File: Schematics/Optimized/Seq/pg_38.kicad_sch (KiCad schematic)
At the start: 67 parts, among them U3901 XBUF64, U3902 XBUF64, U7803 F86

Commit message: Integrate SEQ condensations
Tested: passed expmon_test_seq
Tested: passed run_udiag
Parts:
- renumbered U7803 to U2401
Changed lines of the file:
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@@
   (symbol (lib_id "r1000:F86") (at 482.6 48.26 0) (unit 1)
     (in_bom yes) (on_board yes) (dnp no)
-    (property "Reference" "U7803" (at 495.3 45.72 0)
+    (property "Reference" "U2401" (at 495.3 45.72 0)
       (effects (font (size 1.27 1.27)))
     )
@@
     (instances
       (project "SEQ"
-        (path "/20011966-1ffc-24d7-1b4b-436a182362c4/20011966-47af-2163-0df3-3d84c5f3c1ad"
-          (reference "U7803") (unit 1)
-        )
         (path "/20011966-1ffc-24d7-1b4b-436a182362c4/20011966-7b9d-2905-5287-11179446946c"
           (reference "U2401") (unit 1)

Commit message: Merge SEQ changes
Tested: passed run_udiag
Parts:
- added GF140, GF142, GF144, GF146, GF160, GF162, GF164, GF166, GF296: GF, symbol r1000:GF
- added U4010: F521, symbol r1000:F521
- added U4011: F51, symbol r1000:F51
- added U4012: F37, symbol r1000:F37
- added U5: F244, symbol r1000:F244
- added U6: XPAR64, symbol r1000:XPAR64
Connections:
- net PD: now also U4010.1 (E), U6.1 (ODD)
- net TYPE_DRV~: now also U4012.3 (Q), U5.1 (OE0), U5.19 (OE1)
- net TYPE~0: now also U6.2 (I0)
- net TYPE~1: now also U6.3 (I1)
- net TYPE~10: now also U6.12 (I10)
- net TYPE~11: now also U6.13 (I11)
- net TYPE~12: now also U6.14 (I12)
- net TYPE~13: now also U6.15 (I13)
- net TYPE~14: now also U6.16 (I14)
- net TYPE~15: now also U6.17 (I15)
- net TYPE~16: now also U6.18 (I16)
- net TYPE~17: now also U6.19 (I17)
- net TYPE~18: now also U6.20 (I18)
- net TYPE~19: now also U6.21 (I19)
- net TYPE~2: now also U6.4 (I2)
- net TYPE~20: now also U6.22 (I20)
- net TYPE~21: now also U6.23 (I21)
- net TYPE~22: now also U6.24 (I22)
- net TYPE~23: now also U6.25 (I23)
- net TYPE~24: now also U6.26 (I24)
- net TYPE~25: now also U6.27 (I25)
- net TYPE~26: now also U6.28 (I26)
- net TYPE~27: now also U6.29 (I27)
- net TYPE~28: now also U6.30 (I28)
- net TYPE~29: now also U6.31 (I29)
- net TYPE~3: now also U6.5 (I3)
- net TYPE~30: now also U6.32 (I30)
- net TYPE~31: now also U6.33 (I31)
- net TYPE~32: now also U6.34 (I32)
- net TYPE~33: now also U6.35 (I33)
- net TYPE~34: now also U6.36 (I34)
- net TYPE~35: now also U6.37 (I35)
- net TYPE~36: now also U6.38 (I36)
- net TYPE~37: now also U6.39 (I37)
- net TYPE~38: now also U6.40 (I38)
- net TYPE~39: now also U6.41 (I39)
- net TYPE~4: now also U6.6 (I4)
- net TYPE~40: now also U6.42 (I40)
- net TYPE~41: now also U6.43 (I41)
- net TYPE~42: now also U6.44 (I42)
- net TYPE~43: now also U6.45 (I43)
- net TYPE~44: now also U6.46 (I44)
- net TYPE~45: now also U6.47 (I45)
- net TYPE~46: now also U6.48 (I46)
- net TYPE~47: now also U6.49 (I47)
- net TYPE~48: now also U6.50 (I48)
- net TYPE~49: now also U6.51 (I49)
- net TYPE~5: now also U6.7 (I5)
- net TYPE~50: now also U6.52 (I50)
- net TYPE~51: now also U6.53 (I51)
- net TYPE~52: now also U6.54 (I52)
- net TYPE~53: now also U6.55 (I53)
- net TYPE~54: now also U6.56 (I54)
- net TYPE~55: now also U6.57 (I55)
- net TYPE~56: now also U6.58 (I56)
- net TYPE~57: now also U6.59 (I57)
- net TYPE~58: now also U6.60 (I58)
- net TYPE~59: now also U6.61 (I59)
- net TYPE~6: now also U6.8 (I6)
- net TYPE~60: now also U6.62 (I60)
- net TYPE~61: now also U6.63 (I61)
- net TYPE~62: now also U6.64 (I62)
- net TYPE~63: now also U6.65 (I63)
- net TYPE~7: now also U6.9 (I7)
- net TYPE~8: now also U6.10 (I8)
- net TYPE~9: now also U6.11 (I9)
- new net: U4011.7 (Q), U4012.1 (D0)
- new net BUS_OFF.DIAG: U4011.6 (B3)
- new net Q.SEQ_TV.EN~: GF296.1, U4011.1 (A1)
- new net Q.TYPE.P0: GF166.1, U4010.2 (A0), U5.18 (Y0)
- new net Q.TYPE.P1: GF164.1, U4010.4 (A1), U5.16 (Y1)
- new net Q.TYPE.P2: GF162.1, U4010.6 (A2), U5.14 (Y2)
- new net Q.TYPE.P3: GF160.1, U4010.8 (A3), U5.12 (Y3)
- new net Q.TYPE.P4: GF146.1, U4010.11 (A4), U5.9 (Y4)
- new net Q.TYPE.P5: GF144.1, U4010.13 (A5), U5.7 (Y5)
- new net Q.TYPE.P6: GF142.1, U4010.15 (A6), U5.5 (Y6)
- new net Q.TYPE.P7: GF140.1, U4010.17 (A7), U5.3 (Y7)
- new net Q1~: U4012.2 (D1)
- new net TYPE_POD0: U4010.3 (B0), U5.2 (I0), U6.66 (P0)
- new net TYPE_POD1: U4010.5 (B1), U5.4 (I1), U6.67 (P1)
- new net TYPE_POD2: U4010.7 (B2), U5.6 (I2), U6.68 (P2)
- new net TYPE_POD3: U4010.9 (B3), U5.8 (I3), U6.69 (P3)
- new net TYPE_POD4: U4010.12 (B4), U5.11 (I4), U6.70 (P4)
- new net TYPE_POD5: U4010.14 (B5), U5.13 (I5), U6.71 (P5)
- new net TYPE_POD6: U4010.16 (B6), U5.15 (I6), U6.72 (P6)
- new net TYPE_POD7: U4010.18 (B7), U5.17 (I7), U6.73 (P7)
- new net TYP_ON.DIAG~: U4011.3 (A3), U4011.4 (B1)
- new net TYP_PERR.MCHK: U4010.19 (A=B)
- no-connect marks 0 -> 3
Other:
- moved on the sheet: GF108, GF110, GF112, GF114, GF12, GF124, GF126, GF128, GF130, GF14, GF16, GF176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

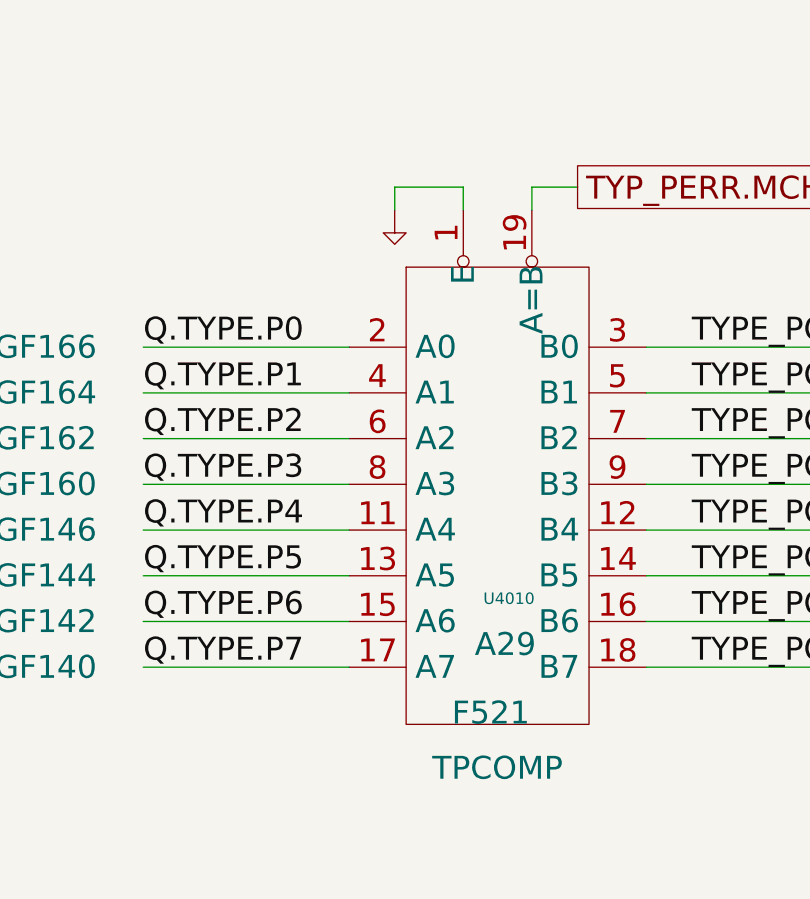
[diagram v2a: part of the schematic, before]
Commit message: Condensation of SEQ, TYP & VAL conditions
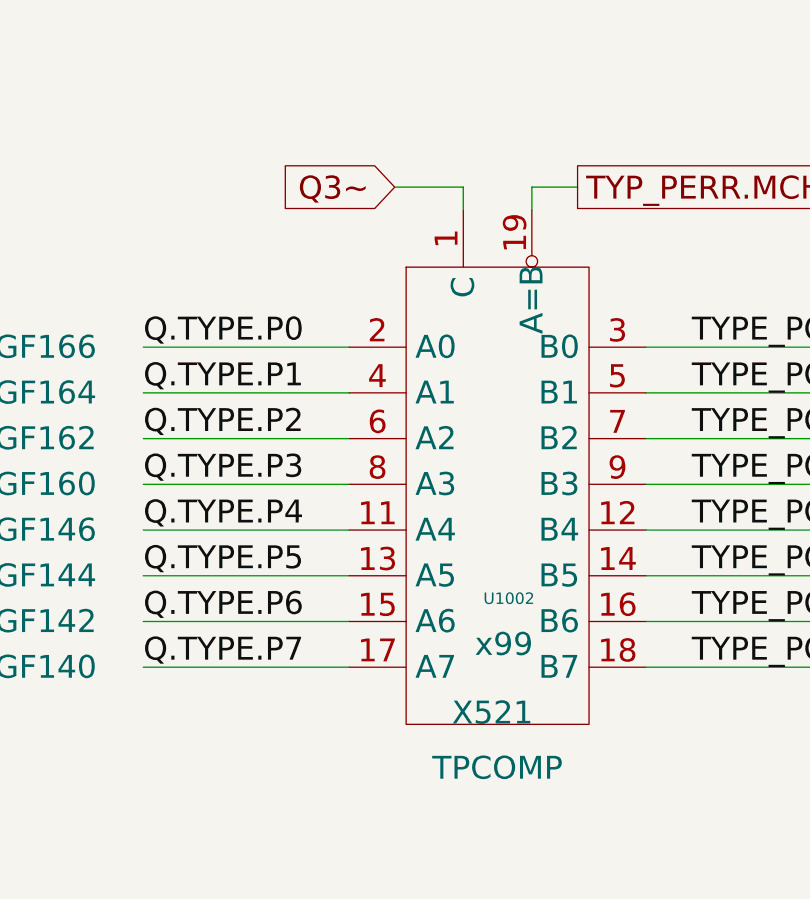
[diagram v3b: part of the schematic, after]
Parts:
- removed U4010: F521, symbol r1000:F521
- added U1002: X521, symbol r1000:X521
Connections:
- net Q.TYPE.P0: now also U1002.2 (A0)
- net Q.TYPE.P1: now also U1002.4 (A1)
- net Q.TYPE.P2: now also U1002.6 (A2)
- net Q.TYPE.P3: now also U1002.8 (A3)
- net Q.TYPE.P4: now also U1002.11 (A4)
- net Q.TYPE.P5: now also U1002.13 (A5)
- net Q.TYPE.P6: now also U1002.15 (A6)
- net Q.TYPE.P7: now also U1002.17 (A7)
- net TYPE_POD0: now also U1002.3 (B0)
- net TYPE_POD1: now also U1002.5 (B1)
- net TYPE_POD2: now also U1002.7 (B2)
- net TYPE_POD3: now also U1002.9 (B3)
- net TYPE_POD4: now also U1002.12 (B4)
- net TYPE_POD5: now also U1002.14 (B5)
- net TYPE_POD6: now also U1002.16 (B6)
- net TYPE_POD7: now also U1002.18 (B7)
- net TYP_PERR.MCHK: now also U1002.19 (A=B)
- new net Q3~: U1002.1 (C)
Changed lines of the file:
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@@
     (stroke (width 0) (type default))
   )
-  (wire (pts (xy 492.76 109.22) (xy 492.76 106.68))
-    (stroke (width 0) (type default))
-  )
   (wire (pts (xy 139.7 109.22) (xy 109.22 109.22))
     (stroke (width 0) (type default))
@@
     )
   )
+  (global_label "Q3~" (shape input) (at 492.76 106.68 180) (fields_autoplaced)
+    (effects (font (size 2.54 2.54)) (justify right))
+    (property "Intersheetrefs" "${INTERSHEET_REFS}" (at 479.8647 106.68 0)
+      (effects (font (size 1.27 1.27)) (justify right))
+    )
+  )
   (global_label "TYP_PERR.MCHK" (shape output) (at 513.08 106.68 0) (fields_autoplaced)
     (effects (font (size 2.54 2.54)) (justify left))
@@
     )
   )
+  (symbol (lib_id "r1000:X521") (at 502.92 157.48 0) (unit 1)
+    (in_bom yes) (on_board yes) (dnp no)
+    (property "Reference" "U1002" (at 505.46 152.4 0)
+      (effects (font (size 1.27 1.27)))
+    )
+    (property "Value" "X521" (at 499.11 165.1 0)
+      (effects (font (size 2.54 2.54)) (justify left))
+    )
+    (property "Footprint" "" (at 504.19 158.75 0)
+      (effects (font (size 1.27 1.27)) hide)
+    )
+    (property "Datasheet" "" (at 504.19 158.75 0)
+      (effects (font (size 1.27 1.27)) hide)
+    )
+    (property "Location" "x99" (at 501.65 157.48 0)
+      (effects (font (size 2.54 2.54)) (justify left))
+    )
+    (property "Name" "TPCOMP" (at 504.19 172.72 0)
+      (effects (font (size 2.54 2.54)) (justify bottom))
+    )
+    (pin "1")
+    (pin "11")
+    (pin "12")
+    (pin "13")
+    (pin "14")
+    (pin "15")
+    (pin "16")
+    (pin "17")
+    (pin "18")
+    (pin "19")
+    (pin "2")
+    (pin "3")
+    (pin "4")
+    (pin "5")
+    (pin "6")
+    (pin "7")
+    (pin "8")
+    (pin "9")
+    (instances
+      (project "SEQ"
+        (path "/20011966-1ffc-24d7-1b4b-436a182362c4/20011966-7b9d-2905-5287-11179446946c"
+          (reference "U1002") (unit 1)
+        )
+      )
+    )
+  )
   (symbol (lib_id "r1000:GF") (at 444.5 139.7 0) (unit 1)
     (in_bom yes) (on_board yes) (dnp no)
@@
     )
   )
-  (symbol (lib_id "r1000:PD") (at 492.76 109.22 0) (unit 1)
-    (in_bom no) (on_board yes) (dnp no)
-    (property "Reference" "#PWR01502" (at 492.76 109.22 0)
-      (effects (font (size 1.27 1.27)) hide)
-    )
-    (property "Value" "PD" (at 492.76 109.22 0)
-      (effects (font (size 1.27 1.27)) hide)
-    )
-    (property "Footprint" "" (at 492.76 109.22 0)
-      (effects (font (size 1.27 1.27)) hide)
-    )
-    (property "Datasheet" "" (at 492.76 109.22 0)
-      (effects (font (size 1.27 1.27)) hide)
-    )
-    (pin "1")
-    (instances
-      (project "SEQ"
-        (path "/20011966-1ffc-24d7-1b4b-436a182362c4/20011966-7b9d-2905-5287-11179446946c"
-          (reference "#PWR01502") (unit 1)
-        )
-      )
-    )
-  )
   (symbol (lib_id "r1000:GF") (at 139.7 129.54 0) (unit 1)
     (in_bom yes) (on_board yes) (dnp no)
@@
         )
       )
-    )
-  )
-  (symbol (lib_id "r1000:F521") (at 502.92 157.48 0) (unit 1)
-    (in_bom yes) (on_board yes) (dnp no)
-    (property "Reference" "U4010" (at 505.46 152.4 0)
-      (effects (font (size 1.27 1.27)))
-    )
-    (property "Value" "F521" (at 499.11 165.1 0)
-      (effects (font (size 2.54 2.54)) (justify left))
-    )
-    (property "Footprint" "" (at 504.19 158.75 0)
-      (effects (font (size 1.27 1.27)) hide)
-    )
-    (property "Datasheet" "" (at 504.19 158.75 0)
-      (effects (font (size 1.27 1.27)) hide)
-    )
-    (property "Location" "A29" (at 501.65 157.48 0)
-      (effects (font (size 2.54 2.54)) (justify left))
-    )
-    (property "Name" "TPCOMP" (at 504.19 172.72 0)
-      (effects (font (size 2.54 2.54)) (justify bottom))
-    )
-    (pin "1")
-    (pin "11")
-    (pin "12")
-    (pin "13")
-    (pin "14")
-    (pin "15")
-    (pin "16")
-    (pin "17")
-    (pin "18")
-    (pin "19")
-    (pin "2")
-    (pin "3")
-    (pin "4")
-    (pin "5")
-    (pin "6")
-    (pin "7")
-    (pin "8")
-    (pin "9")
-    (instances
-      (project "SEQ"
-        (path "/20011966-1ffc-24d7-1b4b-436a182362c4/20011966-7b9d-2905-5287-11179446946c"
-          (reference "U4010") (unit 1)
-        )
-      )

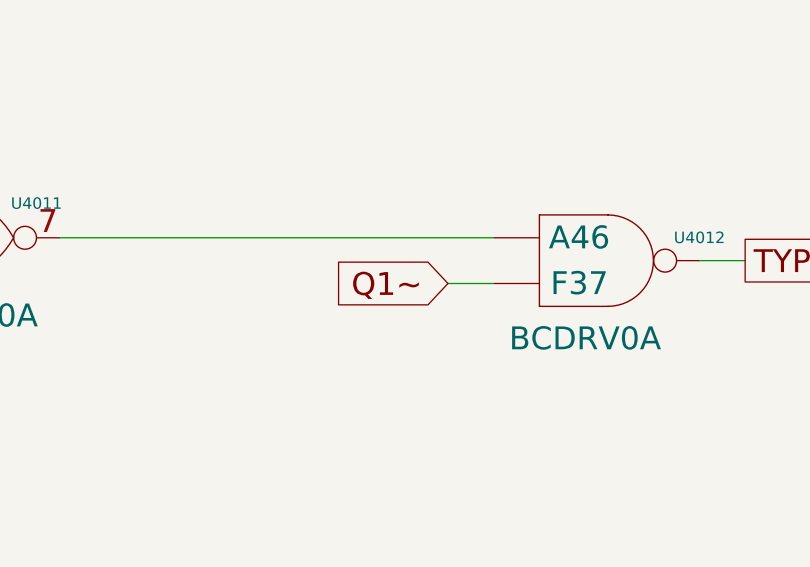
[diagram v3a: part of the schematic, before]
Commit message: Condense Memory Monitor
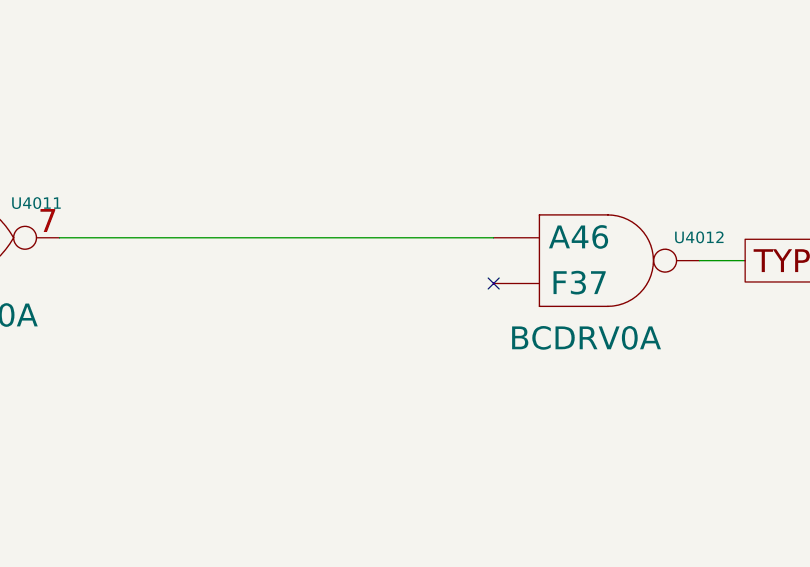
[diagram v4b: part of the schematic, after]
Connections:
- net Q1~: no longer names the net of U4012.2 (D1)
- no-connect marks 3 -> 4
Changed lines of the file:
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@@
   (no_connect (at 424.18 213.36))
   (no_connect (at 340.36 73.66))
+  (no_connect (at 510.54 226.06))
   (bus_entry (at 259.08 274.32) (size -2.54 2.54)
     (stroke (width 0) (type default))
@@
     (stroke (width 0) (type default))
   )
-  (wire (pts (xy 505.46 226.06) (xy 510.54 226.06))
-    (stroke (width 0) (type default))
-  )
   (bus (pts (xy 259.08 294.64) (xy 259.08 299.72))
     (stroke (width 0) (type default))
@@
     )
   )
-  (global_label "Q1~" (shape input) (at 505.46 226.06 180) (fields_autoplaced)
-    (effects (font (size 2.54 2.54)) (justify right))
-    (property "Intersheetrefs" "${INTERSHEET_REFS}" (at 492.5647 226.06 0)
-      (effects (font (size 1.905 1.905)) (justify right))
-    )
-  )

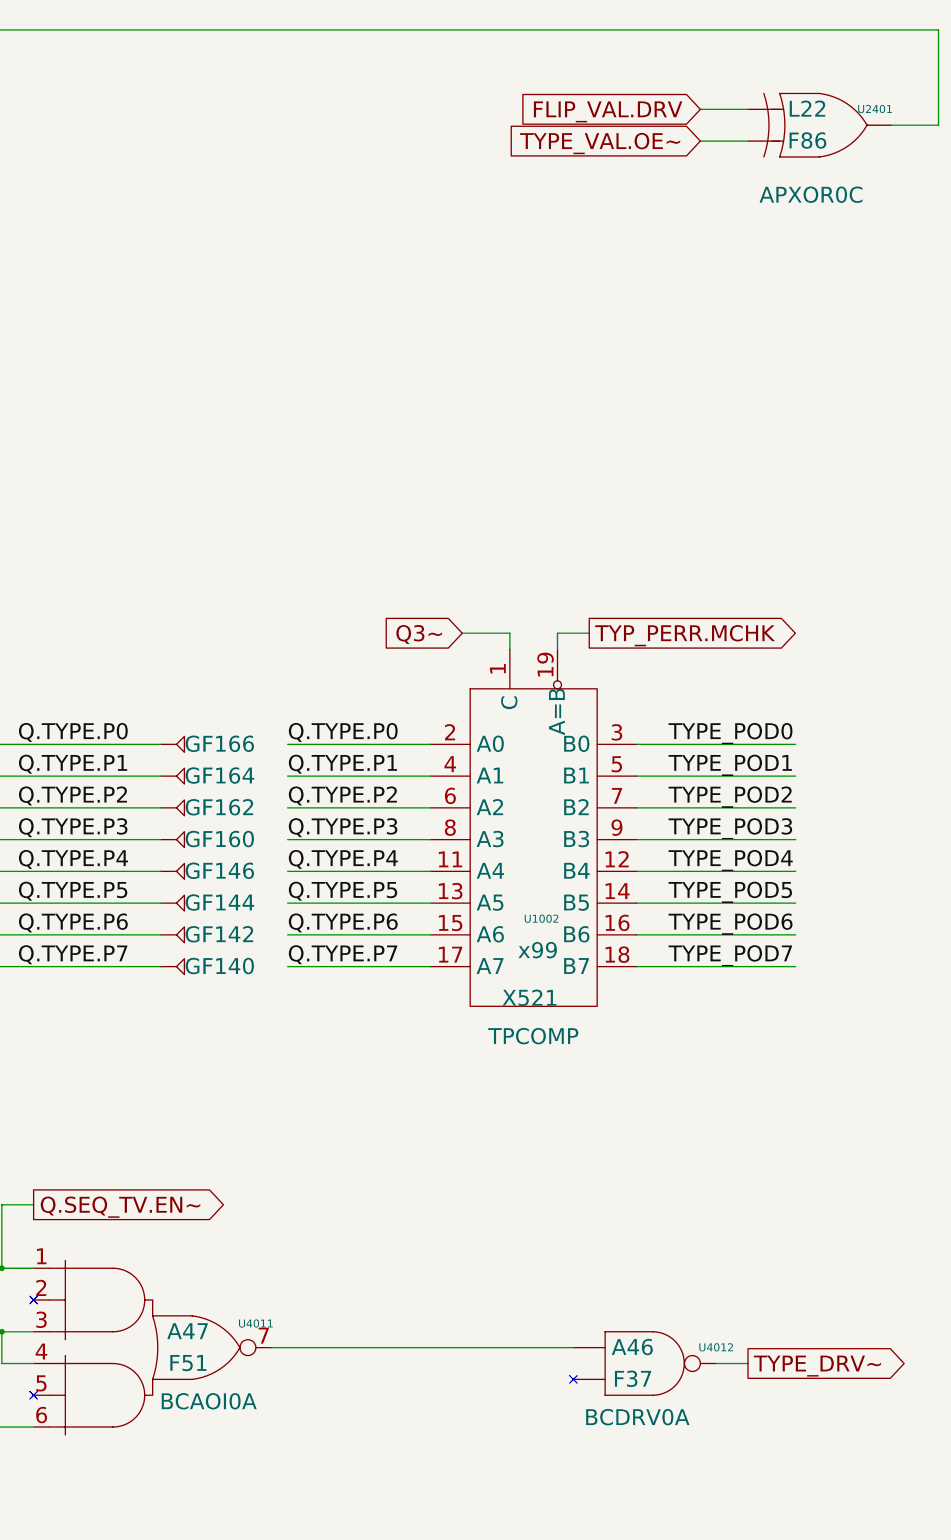
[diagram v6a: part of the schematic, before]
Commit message: Update to kicad9
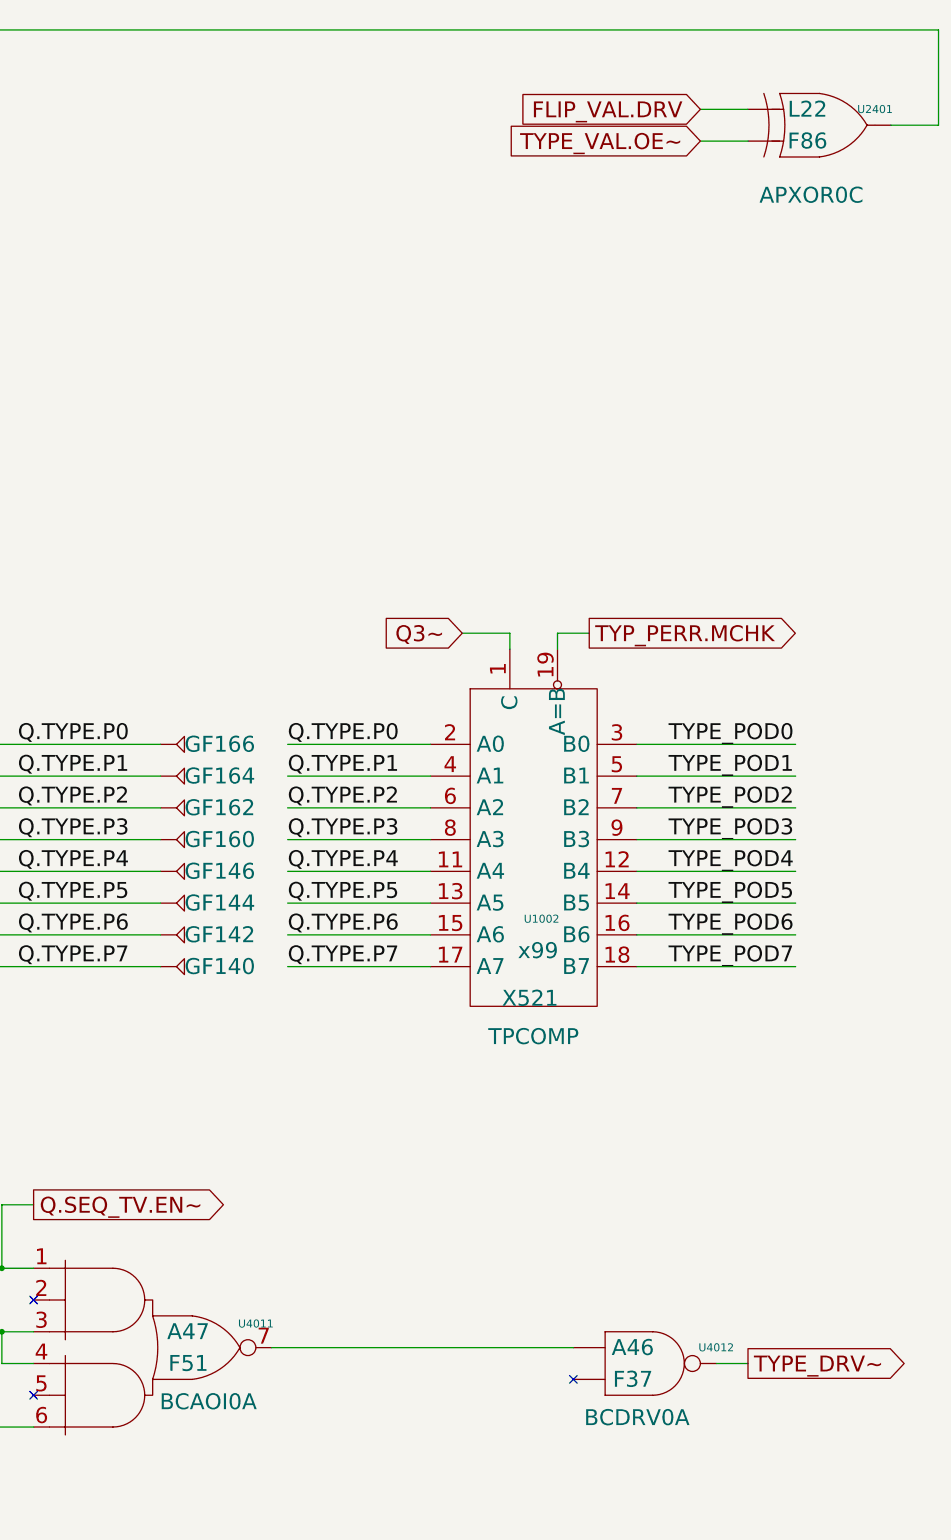
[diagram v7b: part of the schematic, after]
